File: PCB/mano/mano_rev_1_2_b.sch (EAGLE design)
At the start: 54 parts, among them U1 TB6621FNG, U3 TB6621FNG

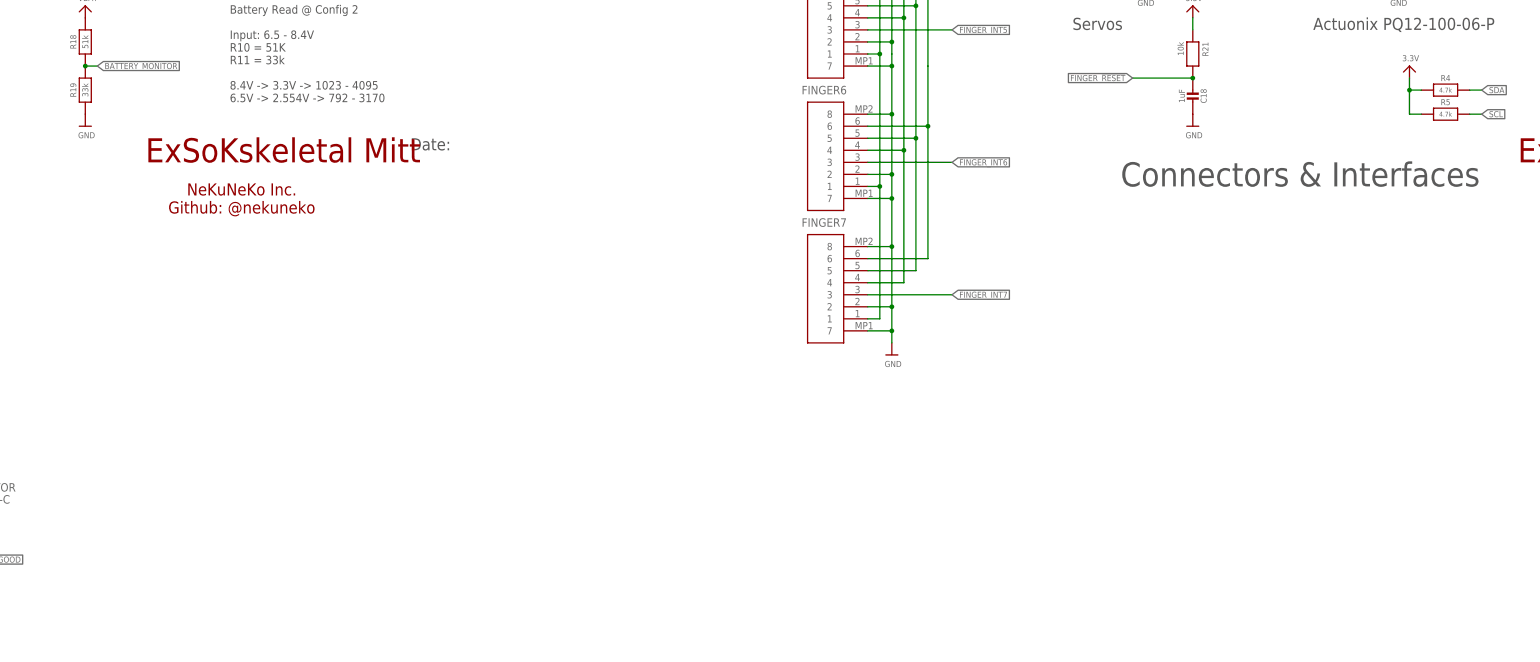
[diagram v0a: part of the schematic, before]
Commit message: Cambio de nombres y ubicación
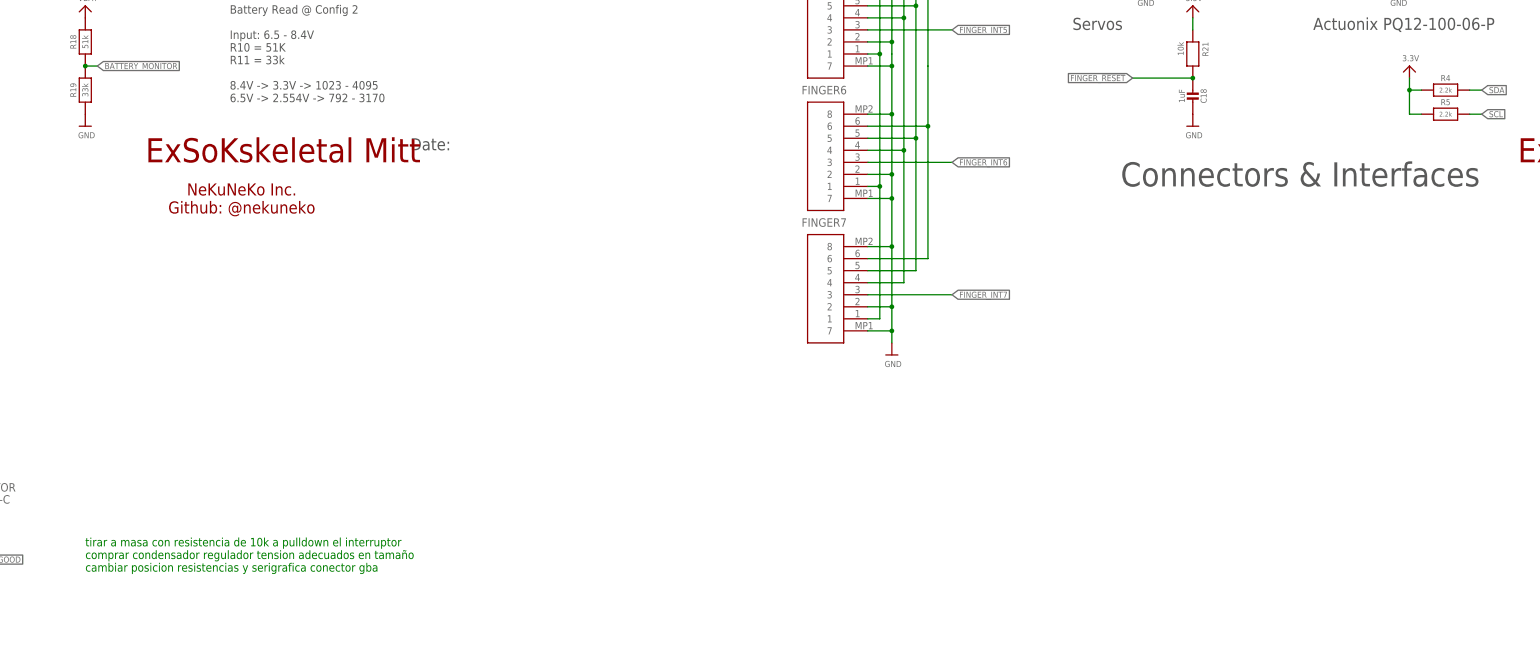
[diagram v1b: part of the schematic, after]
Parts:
- R4, R5: value 4.7k -> 2.2k
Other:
- note added: "tirar a masa con resistencia de 10k a pulldown el interruptor comprar condensador regulador tension adecuados en tamaño cambiar posicion resistencias y serigrafica conector gba"
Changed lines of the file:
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@@
 <part name="BATTERY" library="JST XH Connectors v1-0" deviceset="JST-XH-03-PIN" device="-LONG-PAD"/>
 <part name="U$21" library="microbuilder" deviceset="5.0V" device=""/>
-<part name="R4" library="microbuilder" deviceset="RESISTOR" device="_0603" value="4.7k"/>
-<part name="R5" library="microbuilder" deviceset="RESISTOR" device="_0603" value="4.7k"/>
+<part name="R4" library="microbuilder" deviceset="RESISTOR" device="_0603" value="2.2k"/>
+<part name="R5" library="microbuilder" deviceset="RESISTOR" device="_0603" value="2.2k"/>
 <part name="U$10" library="microbuilder" deviceset="3.3V" device=""/>
 <part name="R6" library="microbuilder" deviceset="RESISTOR" device="_0603" value="10k"/>
@@
 Open or VIN = On
 Closed or Ground = Off (GND)</text>
+<text x="149.86" y="-68.58" size="1.778" layer="91">tirar a masa con resistencia de 10k a pulldown el interruptor
+comprar condensador regulador tension adecuados en tamaño
+cambiar posicion resistencias y serigrafica conector gba
+</text>
 </plain>
 <instances>
